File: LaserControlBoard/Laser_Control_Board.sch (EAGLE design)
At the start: 37 parts, among them J1 Servo, J2 FTDI, J5 FEMALE 2x3, U1 ATMEGA328P, Y1 16MHz

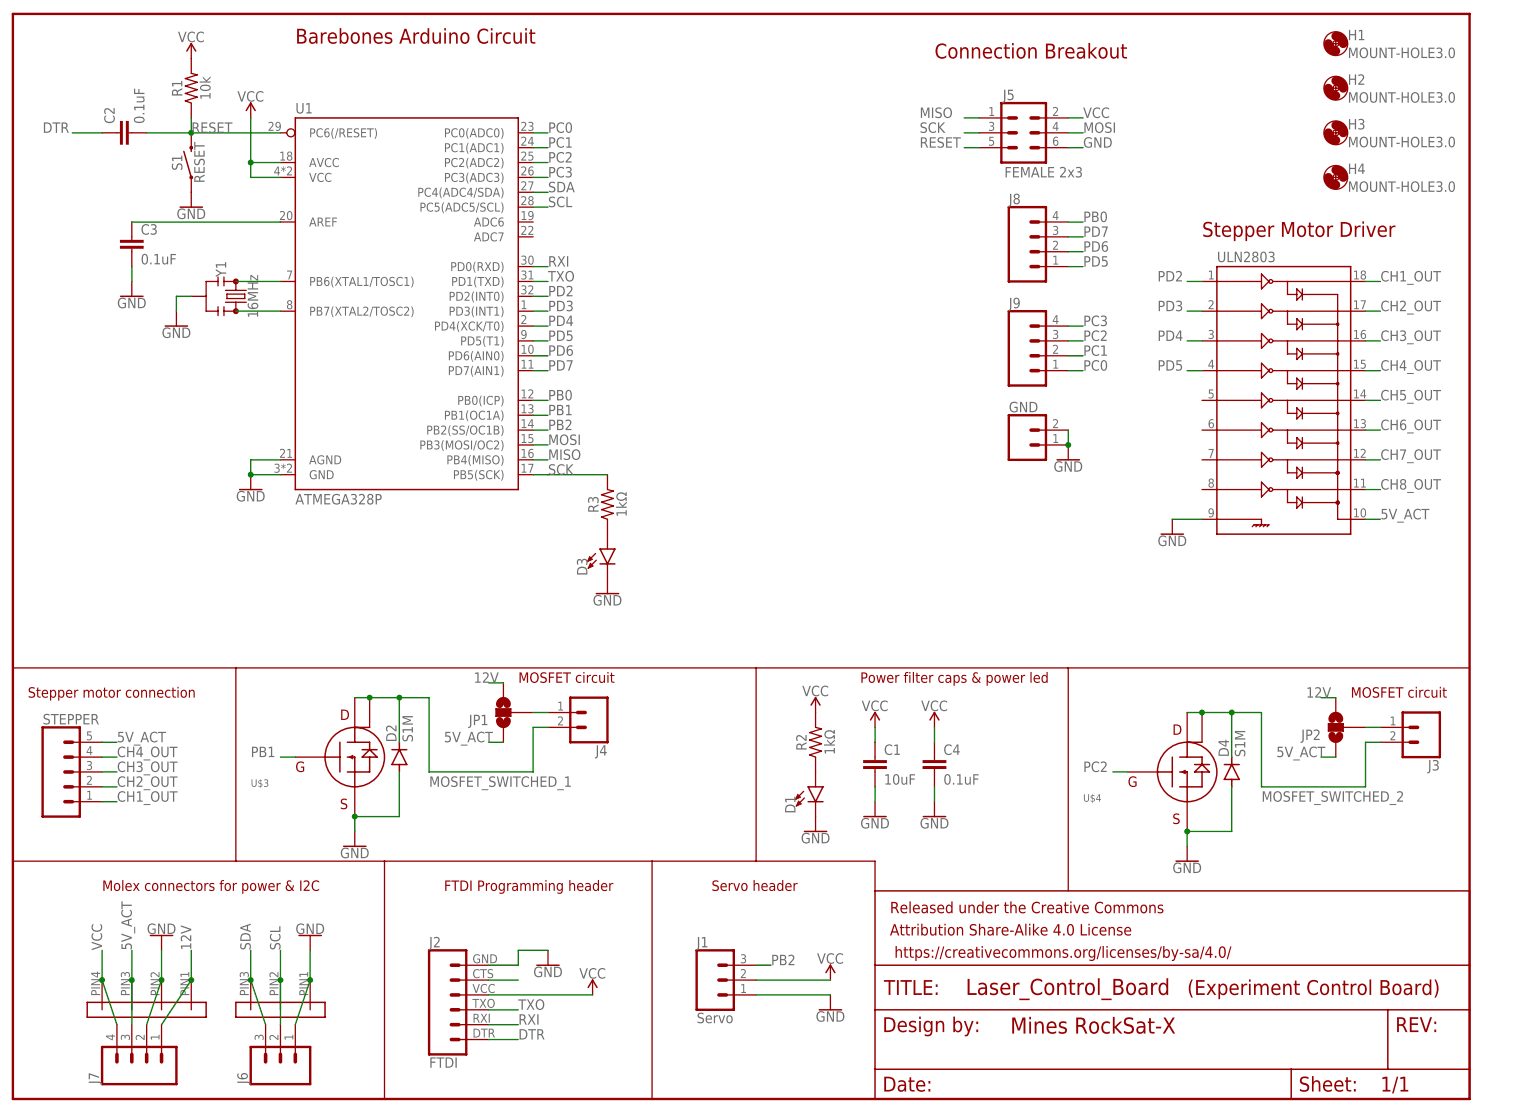
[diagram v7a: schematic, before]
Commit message: Changed silkscreen for clarity
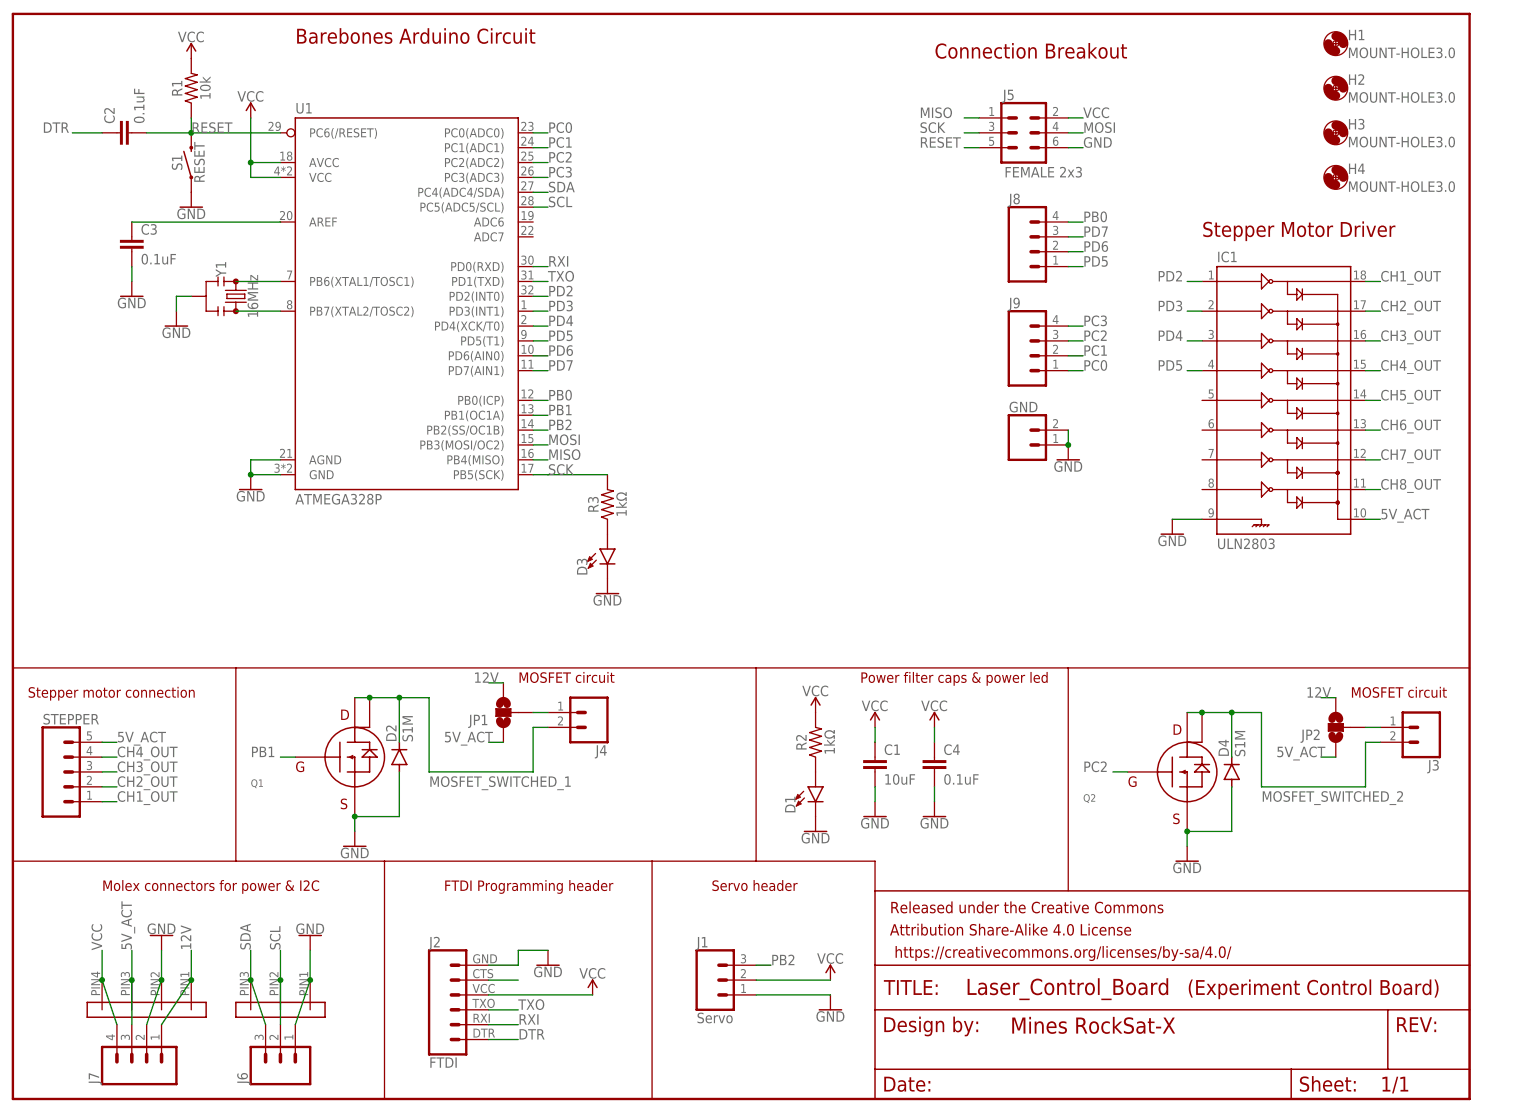
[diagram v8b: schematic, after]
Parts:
- IC1: value (none) -> ULN2803
- renumbered U$3 to Q1, U$4 to Q2, ULN2803 to IC1
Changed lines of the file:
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@@
 <?xml version="1.0" encoding="utf-8"?>
 <!DOCTYPE eagle SYSTEM "eagle.dtd">
-<eagle version="9.5.2">
+<eagle version="9.4.2">
 <drawing>
 <settings>
@@
 <part name="J1" library="SparkFun-Connectors" deviceset="CONN_03" device="" value="Servo"/>
 <part name="J2" library="SparkFun-Connectors" deviceset="6_PIN_SERIAL_CABLE" device="PTH" value="FTDI"/>
-<part name="ULN2803" library="SparkFun-IC-Special-Function" deviceset="ULN2803" device="SOICW"/>
+<part name="IC1" library="SparkFun-IC-Special-Function" deviceset="ULN2803" device="SOICW" value="ULN2803"/>
 <part name="C1" library="SparkFun-Capacitors" deviceset="10UF" device="-0805-10V-10%" value="10uF"/>
 <part name="C2" library="SparkFun-Capacitors" deviceset="2.2UF" device="-0805-25V-(+80/-20%)" value="0.1uF"/>
@@
 <part name="D2" library="diode" library_urn="urn:adsk.eagle:library:210" deviceset="S1M" device="" package3d_urn="urn:adsk.eagle:package:43460/3"/>
 <part name="D1" library="SparkFun-LED" deviceset="LED-GREEN" device="1206"/>
-<part name="U$3" library="PowerManagementParts" deviceset="BUK9880-55A" device="" package3d_urn="urn:adsk.eagle:package:43439/1" value=""/>
+<part name="Q1" library="PowerManagementParts" deviceset="BUK9880-55A" device="" package3d_urn="urn:adsk.eagle:package:43439/1" value=""/>
 <part name="J4" library="SparkFun-Connectors" deviceset="CONN_02" device=""/>
 <part name="GND1" library="SparkFun-PowerSymbols" deviceset="GND" device=""/>
@@
 <part name="J5" library="SparkFun-Connectors" deviceset="CONN_03X2" device="FEMALE" value="FEMALE 2x3"/>
 <part name="D4" library="diode" library_urn="urn:adsk.eagle:library:210" deviceset="S1M" device="" package3d_urn="urn:adsk.eagle:package:43460/3"/>
-<part name="U$4" library="PowerManagementParts" deviceset="BUK9880-55A" device="" package3d_urn="urn:adsk.eagle:package:43439/1" value=""/>
+<part name="Q2" library="PowerManagementParts" deviceset="BUK9880-55A" device="" package3d_urn="urn:adsk.eagle:package:43439/1" value=""/>
 <part name="J3" library="SparkFun-Connectors" deviceset="CONN_02" device=""/>
 <part name="GND15" library="SparkFun-PowerSymbols" deviceset="GND" device=""/>
@@
 <attribute name="NAME" x="71.12" y="25.908" size="1.778" layer="95" font="vector"/>
 </instance>
-<instance part="ULN2803" gate="G$1" x="215.9" y="121.92" smashed="yes">
+<instance part="IC1" gate="G$1" x="215.9" y="121.92" smashed="yes">
 <attribute name="NAME" x="205.74" y="143.002" size="1.778" layer="95"/>
 <attribute name="VALUE" x="205.74" y="93.98" size="1.778" layer="96"/>
@@
 <attribute name="VALUE" x="139.065" y="48.768" size="1.778" layer="96" font="vector" rot="R90" align="top-left"/>
 </instance>
-<instance part="U$3" gate="G$1" x="48.26" y="53.34" smashed="yes">
+<instance part="Q1" gate="G$1" x="48.26" y="53.34" smashed="yes">
 <attribute name="NAME" x="40.64" y="53.34" size="1.27" layer="95"/>
 <attribute name="VALUE" x="40.64" y="50.8" size="1.27" layer="96"/>
@@
 <attribute name="VALUE" x="210.5914" y="58.42" size="1.778" layer="96" rot="R90"/>
 </instance>
-<instance part="U$4" gate="G$1" x="190.5" y="50.8" smashed="yes">
+<instance part="Q2" gate="G$1" x="190.5" y="50.8" smashed="yes">
 <attribute name="NAME" x="182.88" y="50.8" size="1.27" layer="95"/>
 <attribute name="VALUE" x="182.88" y="48.26" size="1.27" layer="96"/>
@@
 </segment>
 <segment>
-<pinref part="ULN2803" gate="G$1" pin="9"/>
+<pinref part="IC1" gate="G$1" pin="9"/>
 <pinref part="GND12" gate="1" pin="GND"/>
 <wire x1="203.2" y1="99.06" x2="198.12" y2="99.06" width="0.1524" layer="91"/>
@@
 <pinref part="D2" gate="G$1" pin="A"/>
 <wire x1="66.04" y1="55.88" x2="66.04" y2="48.26" width="0.1524" layer="91"/>
-<pinref part="U$3" gate="G$1" pin="SOURCE"/>
+<pinref part="Q1" gate="G$1" pin="SOURCE"/>
 <wire x1="66.04" y1="48.26" x2="58.42" y2="48.26" width="0.1524" layer="91"/>
 <wire x1="58.42" y1="48.26" x2="58.42" y2="45.72" width="0.1524" layer="91"/>
@@
 <pinref part="D4" gate="G$1" pin="A"/>
 <wire x1="208.28" y1="53.34" x2="208.28" y2="45.72" width="0.1524" layer="91"/>
-<pinref part="U$4" gate="G$1" pin="SOURCE"/>
+<pinref part="Q2" gate="G$1" pin="SOURCE"/>
 <wire x1="208.28" y1="45.72" x2="200.66" y2="45.72" width="0.1524" layer="91"/>
 <wire x1="200.66" y1="45.72" x2="200.66" y2="43.18" width="0.1524" layer="91"/>
@@
 </segment>
 <segment>
-<pinref part="ULN2803" gate="G$1" pin="10"/>
+<pinref part="IC1" gate="G$1" pin="10"/>
 <wire x1="231.14" y1="99.06" x2="233.68" y2="99.06" width="0.1524" layer="91"/>
 <label x="233.68" y="99.06" size="1.778" layer="95"/>
@@
 <net name="CH1_OUT" class="0">
 <segment>
-<pinref part="ULN2803" gate="G$1" pin="18"/>
+<pinref part="IC1" gate="G$1" pin="18"/>
 <wire x1="231.14" y1="139.7" x2="233.68" y2="139.7" width="0.1524" layer="91"/>
 <label x="233.68" y="139.7" size="1.778" layer="95"/>
@@
 <net name="CH2_OUT" class="0">
 <segment>
-<pinref part="ULN2803" gate="G$1" pin="17"/>
+<pinref part="IC1" gate="G$1" pin="17"/>
 <wire x1="231.14" y1="134.62" x2="233.68" y2="134.62" width="0.1524" layer="91"/>
 <label x="233.68" y="134.62" size="1.778" layer="95"/>
@@
 <net name="CH3_OUT" class="0">
 <segment>
-<pinref part="ULN2803" gate="G$1" pin="16"/>
+<pinref part="IC1" gate="G$1" pin="16"/>
 <wire x1="231.14" y1="129.54" x2="233.68" y2="129.54" width="0.1524" layer="91"/>
 <label x="233.68" y="129.54" size="1.778" layer="95"/>
@@
 <net name="CH4_OUT" class="0">
 <segment>
-<pinref part="ULN2803" gate="G$1" pin="15"/>
+<pinref part="IC1" gate="G$1" pin="15"/>
 <wire x1="231.14" y1="124.46" x2="233.68" y2="124.46" width="0.1524" layer="91"/>
 <label x="233.68" y="124.46" size="1.778" layer="95"/>
@@
 <net name="CH5_OUT" class="0">
 <segment>
-<pinref part="ULN2803" gate="G$1" pin="14"/>
+<pinref part="IC1" gate="G$1" pin="14"/>
 <wire x1="231.14" y1="119.38" x2="233.68" y2="119.38" width="0.1524" layer="91"/>
 <label x="233.68" y="119.38" size="1.778" layer="95"/>
@@
 <net name="CH6_OUT" class="0">
 <segment>
-<pinref part="ULN2803" gate="G$1" pin="13"/>
+<pinref part="IC1" gate="G$1" pin="13"/>
 <wire x1="231.14" y1="114.3" x2="233.68" y2="114.3" width="0.1524" layer="91"/>
 <label x="233.68" y="114.3" size="1.778" layer="95"/>
@@
 <net name="CH7_OUT" class="0">
 <segment>
-<pinref part="ULN2803" gate="G$1" pin="12"/>
+<pinref part="IC1" gate="G$1" pin="12"/>
 <wire x1="231.14" y1="109.22" x2="233.68" y2="109.22" width="0.1524" layer="91"/>
 <label x="233.68" y="109.22" size="1.778" layer="95"/>
@@
 <net name="CH8_OUT" class="0">
 <segment>
-<pinref part="ULN2803" gate="G$1" pin="11"/>
+<pinref part="IC1" gate="G$1" pin="11"/>
 <wire x1="231.14" y1="104.14" x2="233.68" y2="104.14" width="0.1524" layer="91"/>
 <label x="233.68" y="104.14" size="1.778" layer="95"/>
@@
 </segment>
 <segment>
-<pinref part="ULN2803" gate="G$1" pin="1"/>
+<pinref part="IC1" gate="G$1" pin="1"/>
 <wire x1="203.2" y1="139.7" x2="200.66" y2="139.7" width="0.1524" layer="91"/>
 <label x="195.58" y="139.7" size="1.778" layer="95"/>
@@
 </segment>
 <segment>
-<pinref part="ULN2803" gate="G$1" pin="2"/>
+<pinref part="IC1" gate="G$1" pin="2"/>
 <wire x1="203.2" y1="134.62" x2="200.66" y2="134.62" width="0.1524" layer="91"/>
 <label x="195.58" y="134.62" size="1.778" layer="95"/>
@@
 </segment>
 <segment>
-<pinref part="ULN2803" gate="G$1" pin="3"/>
+<pinref part="IC1" gate="G$1" pin="3"/>
 <wire x1="203.2" y1="129.54" x2="200.66" y2="129.54" width="0.1524" layer="91"/>
 <label x="195.58" y="129.54" size="1.778" layer="95"/>
@@
 </segment>
 <segment>
-<pinref part="ULN2803" gate="G$1" pin="4"/>
+<pinref part="IC1" gate="G$1" pin="4"/>
 <wire x1="203.2" y1="124.46" x2="200.66" y2="124.46" width="0.1524" layer="91"/>
 <label x="195.58" y="124.46" size="1.778" layer="95"/>
@@
 </segment>
 <segment>
-<pinref part="U$3" gate="G$1" pin="GATE"/>
+<pinref part="Q1" gate="G$1" pin="GATE"/>
 <wire x1="48.26" y1="58.42" x2="45.72" y2="58.42" width="0.1524" layer="91"/>
 <label x="40.64" y="58.42" size="1.778" layer="95"/>
@@
 <wire x1="88.9" y1="55.88" x2="71.12" y2="55.88" width="0.1524" layer="91"/>
 <label x="71.12" y="53.34" size="1.778" layer="95"/>
-<pinref part="U$3" gate="G$1" pin="DRAIN"/>
-<pinref part="U$3" gate="G$1" pin="DRAIN_TAB"/>
+<pinref part="Q1" gate="G$1" pin="DRAIN"/>
+<pinref part="Q1" gate="G$1" pin="DRAIN_TAB"/>
 <wire x1="58.42" y1="68.58" x2="60.96" y2="68.58" width="0.1524" layer="91"/>
 <wire x1="60.96" y1="68.58" x2="66.04" y2="68.58" width="0.1524" layer="91"/>
@@
 <net name="MOSFET_SWITCHED_2" class="0">
 <segment>
-<pinref part="U$4" gate="G$1" pin="DRAIN"/>
-<pinref part="U$4" gate="G$1" pin="DRAIN_TAB"/>
+<pinref part="Q2" gate="G$1" pin="DRAIN"/>
+<pinref part="Q2" gate="G$1" pin="DRAIN_TAB"/>
 <wire x1="200.66" y1="66.04" x2="203.2" y2="66.04" width="0.1524" layer="91"/>
 <wire x1="203.2" y1="66.04" x2="208.28" y2="66.04" width="0.1524" layer="91"/>
@@
 </segment>
 <segment>
-<pinref part="U$4" gate="G$1" pin="GATE"/>
+<pinref part="Q2" gate="G$1" pin="GATE"/>
 <wire x1="190.5" y1="55.88" x2="187.96" y2="55.88" width="0.1524" layer="91"/>
 <label x="182.88" y="55.88" size="1.778" layer="95"/>
